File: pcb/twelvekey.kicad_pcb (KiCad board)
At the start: 2 copper layers, 75.2 x 62.6 mm, 54 parts, among them J1 Conn_01x06, Q1 AO3401A, U1 ATmega328P-AU, U2 SRV05-4, X1 Crystal_GND24_Small

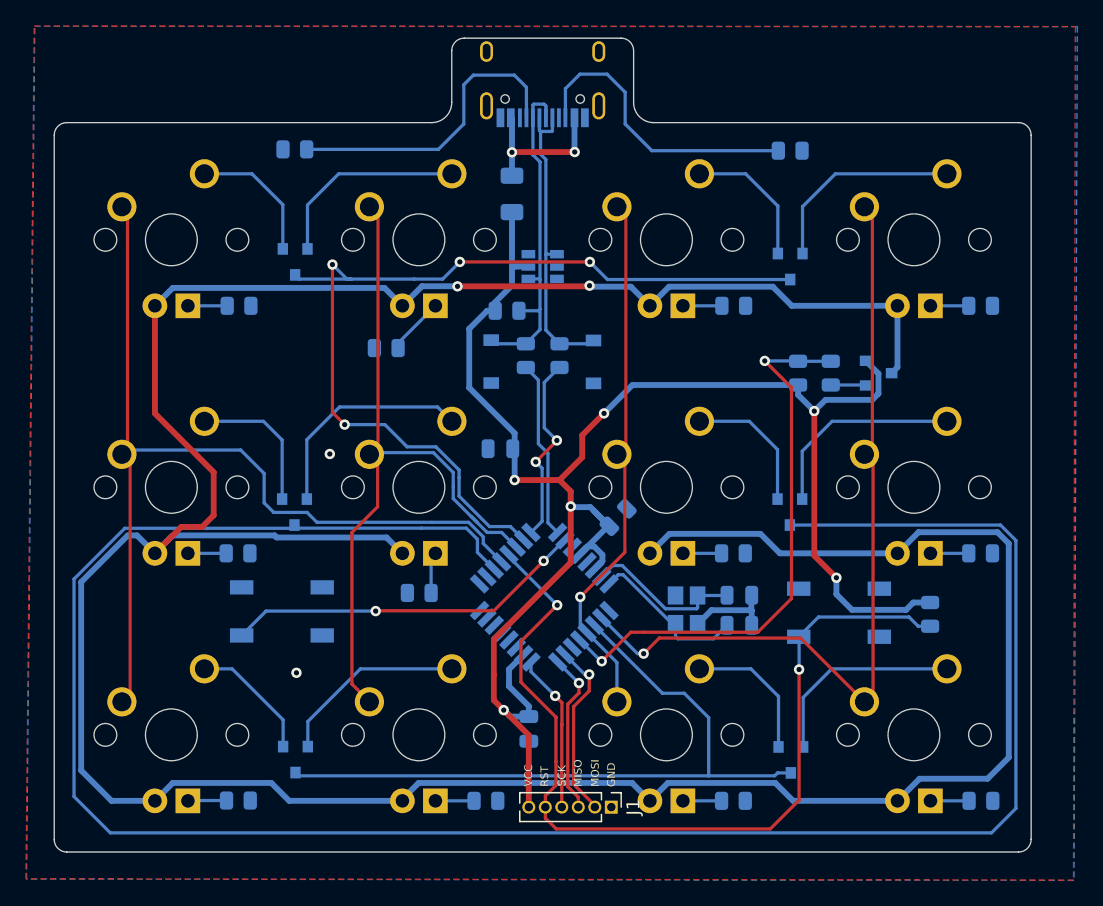
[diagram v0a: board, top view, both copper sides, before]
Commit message: update PCB files for KiCAD 8.0
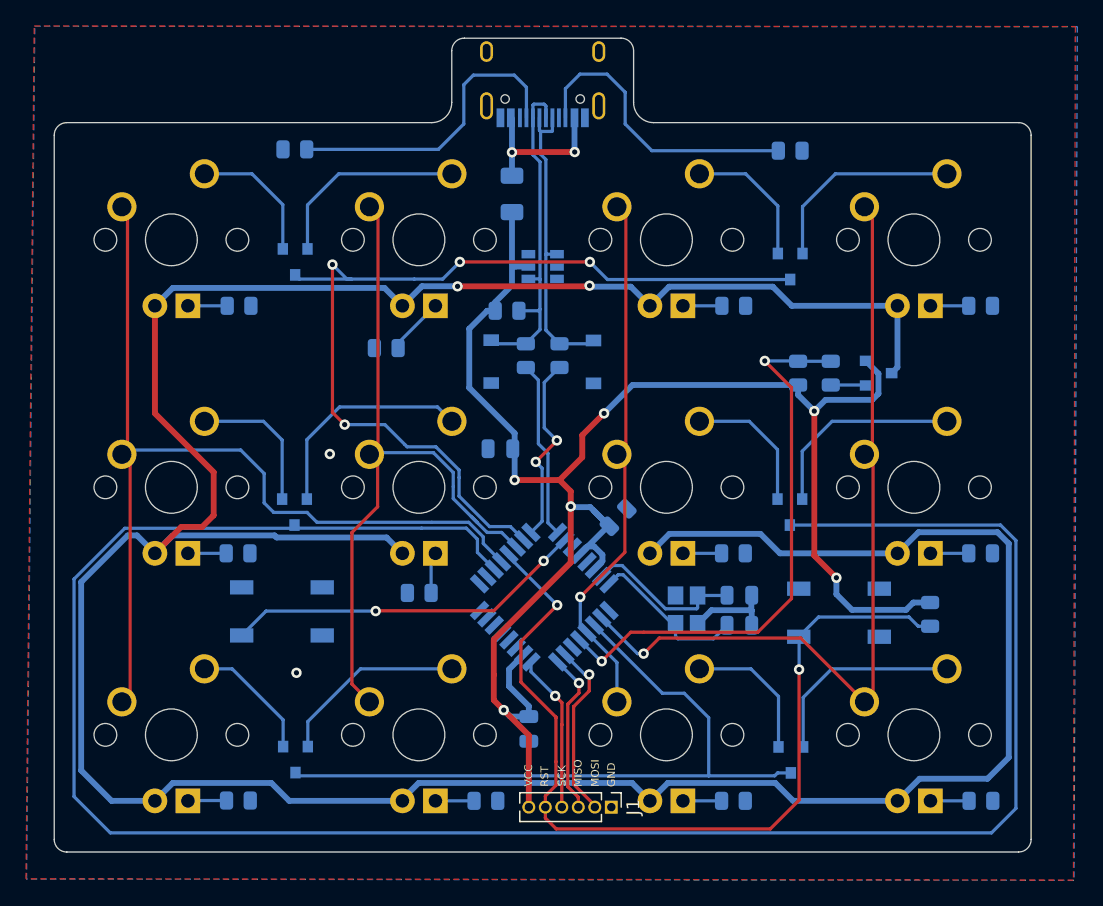
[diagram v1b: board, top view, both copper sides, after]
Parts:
- R19: value 100r -> 100R
- U1: value ATmega328P-AU -> ATmega328P-A
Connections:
- U1 pad 14: Net-(U1-Pad14) -> unconnected-(U1-PB2-Pad14)
- U1 pad 19: Net-(U1-Pad19) -> unconnected-(U1-ADC6-Pad19)
- U1 pad 20: Net-(U1-Pad20) -> unconnected-(U1-AREF-Pad20)
- U1 pad 22: Net-(U1-Pad22) -> unconnected-(U1-ADC7-Pad22)
- U1 pad 23: Net-(U1-Pad23) -> unconnected-(U1-PC0-Pad23)
- U1 pad 24: Net-(U1-Pad24) -> unconnected-(U1-PC1-Pad24)
- U1 pad 25: Net-(U1-Pad25) -> unconnected-(U1-PC2-Pad25)
- U1 pad 26: Net-(U1-Pad26) -> unconnected-(U1-PC3-Pad26)
- U1 pad 9: Net-(U1-Pad9) -> unconnected-(U1-PD5-Pad9)
- U2 pad 3: Net-(U2-Pad3) -> unconnected-(U2-IO2-Pad3)
- U2 pad 6: Net-(U2-Pad6) -> unconnected-(U2-IO4-Pad6)
- USB1 pad A8: Net-(USB1-PadA8) -> unconnected-(USB1-SBU1-PadA8)
- USB1 pad B8: Net-(USB1-PadB8) -> unconnected-(USB1-SBU2-PadB8)
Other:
- net class Default removed
- net class Power removed
